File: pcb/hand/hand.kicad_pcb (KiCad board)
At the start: 2 copper layers, 149.5 x 99.8 mm, 35 parts, among them J1 Conn_01x15, J2 Conn_01x15

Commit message: pcb/hand Begin tidying DRC.
TODO:
- Name
- Date
- Connect J1 to J2
- Finish DRC
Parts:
- renumbered REF** to H1, REF** to H2, REF** to H3, REF** to H4
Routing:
- net col5: track 91.3 -> 121.7 mm
- net col1: track 173.0 -> 198.4 mm
- net col3: track 133.1 -> 158.6 mm
- net col2: track 159.3 -> 184.7 mm
- net col4: track 121.8 -> 147.1 mm
- net col0: track 167.1 -> 186.2 mm
- net row2: track 162.9 -> 176.7 mm
- net row3: track 185.7 -> 197.7 mm
- net row0: track 184.5 -> 193.6 mm
- net row1: track 148.1 -> 157.0 mm
- net col6: track 45.1 -> 52.3 mm

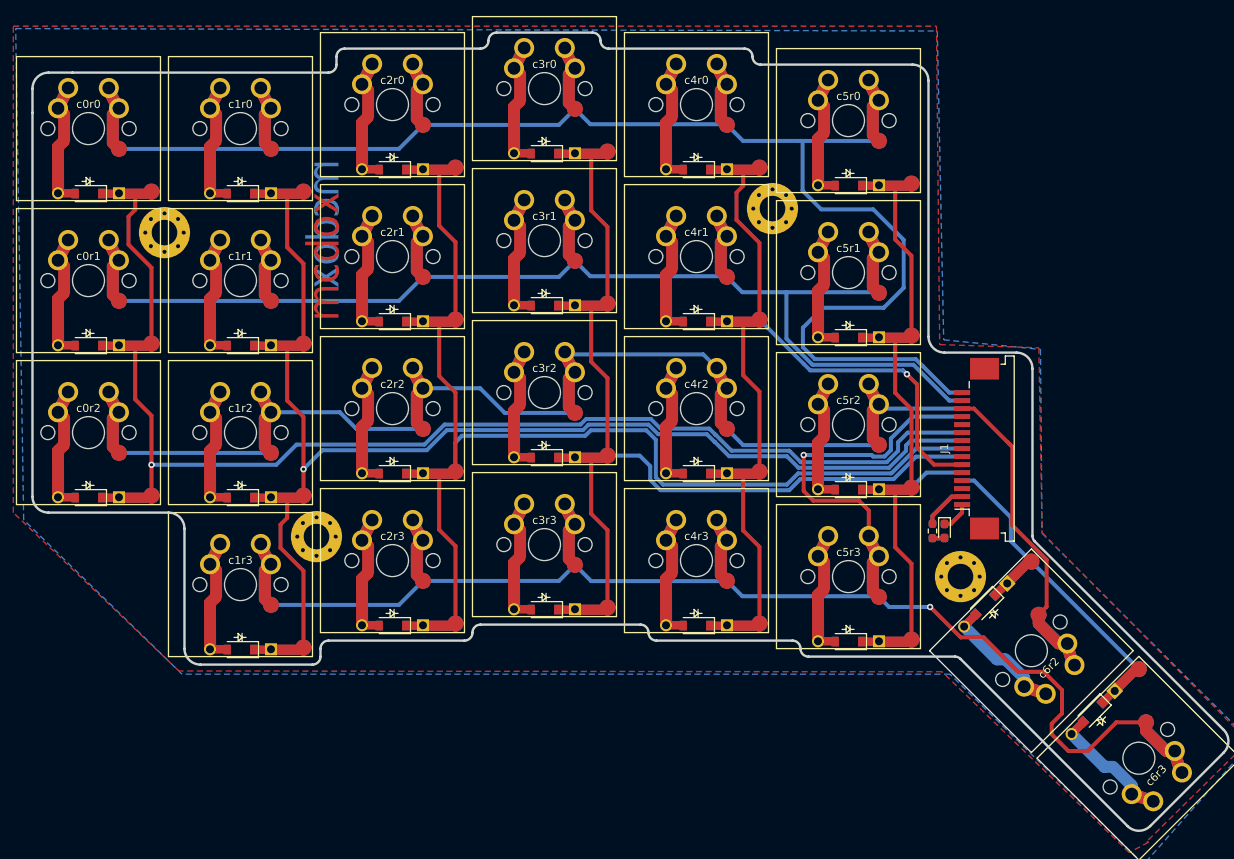
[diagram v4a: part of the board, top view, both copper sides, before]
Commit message: pcb/hand Recess cutout under switches on Eco2.User
Remove all the pad-to-pad tracks too... Loads of them!
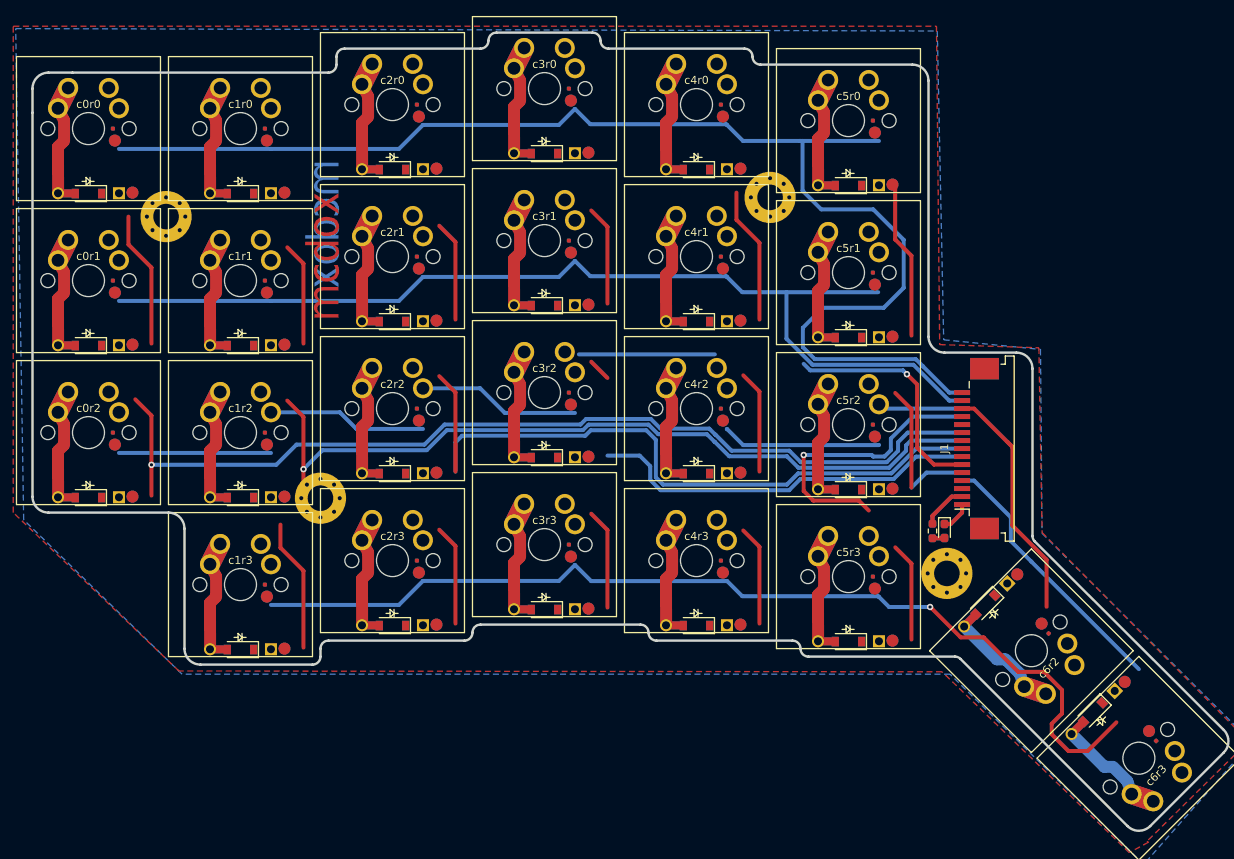
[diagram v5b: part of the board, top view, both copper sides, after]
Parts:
- H1, H2, H3, H4: footprint MountingHole:MountingHole_3.2mm_M3_Pad_Via -> hand:MountingHole_3.2mm_M3_Pad_Via
- moved H2 4.83 mm to (36.0, 53.2)
- moved H1 2.01 mm to (16.7, 18.0)
- moved H4 1.75 mm to (114.3, 62.6)
- moved H3 1.43 mm to (92.2, 15.6)
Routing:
- net col3: track 158.6 -> 76.8 mm
- net col4: track 147.1 -> 72.1 mm
- net col2: track 184.7 -> 113.0 mm
- net col5: track 121.7 -> 51.8 mm
- net col1: track 198.4 -> 130.8 mm
- net col0: track 186.2 -> 138.0 mm
- net row2: track 176.7 -> 136.5 mm
- net row3: track 197.7 -> 160.4 mm
- net row0: track 193.6 -> 165.5 mm
- net row1: track 157.0 -> 129.6 mm
- net col6: track 52.3 -> 33.6 mm

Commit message: pcb/hand Full layout.
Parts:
- moved R1 4.33 mm to (113.0, 53.0), turned to 180 degrees
- moved R2 4.33 mm to (113.0, 53.0), turned to 180 degrees
- moved LED1 2.97 mm to (113.0, 54.5), turned to 180 degrees
- moved LED2 2.97 mm to (113.0, 54.5), turned to 180 degrees
- moved H4 0.40 mm to (114.3, 63.0)
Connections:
- J1 pad 11: (no net) -> row4_NC
- J1 pad 3: (no net) -> col7_NC
- J2 pad 13: (no net) -> col7_NC
- J2 pad 5: (no net) -> row4_NC
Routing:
- net row2: track 136.5 -> 237.7 mm, vias 0 -> 1
- net row3: track 160.4 -> 246.1 mm, vias 2 -> 3
- net col3: track 76.8 -> 155.6 mm, vias 0 -> 1
- net row1: track 129.6 -> 208.1 mm, vias 0 -> 1
- net col4: track 72.1 -> 142.4 mm, vias 1 -> 2
- net col2: track 113.0 -> 177.4 mm, vias 0 -> 1
- net col1: track 130.8 -> 194.8 mm
- net col5: track 51.8 -> 112.7 mm, vias 0 -> 1
- net row0: track 165.5 -> 216.8 mm, vias 0 -> 1
- net col0: track 138.0 -> 185.6 mm
- net col6: track 33.6 -> 55.0 mm, vias 0 -> 1
- net row4_NC: track 0.00 -> 3.60 mm, vias 0 -> 1
- net col7_NC: track 0.00 -> 3.60 mm, vias 0 -> 1
- net +3V3: track 11.4 -> 9.18 mm, vias 0 -> 1
- net GND: track 7.58 -> 8.66 mm, vias 0 -> 1
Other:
- board text added: "Dave McEwan"
- board text added: "Feb 2023"

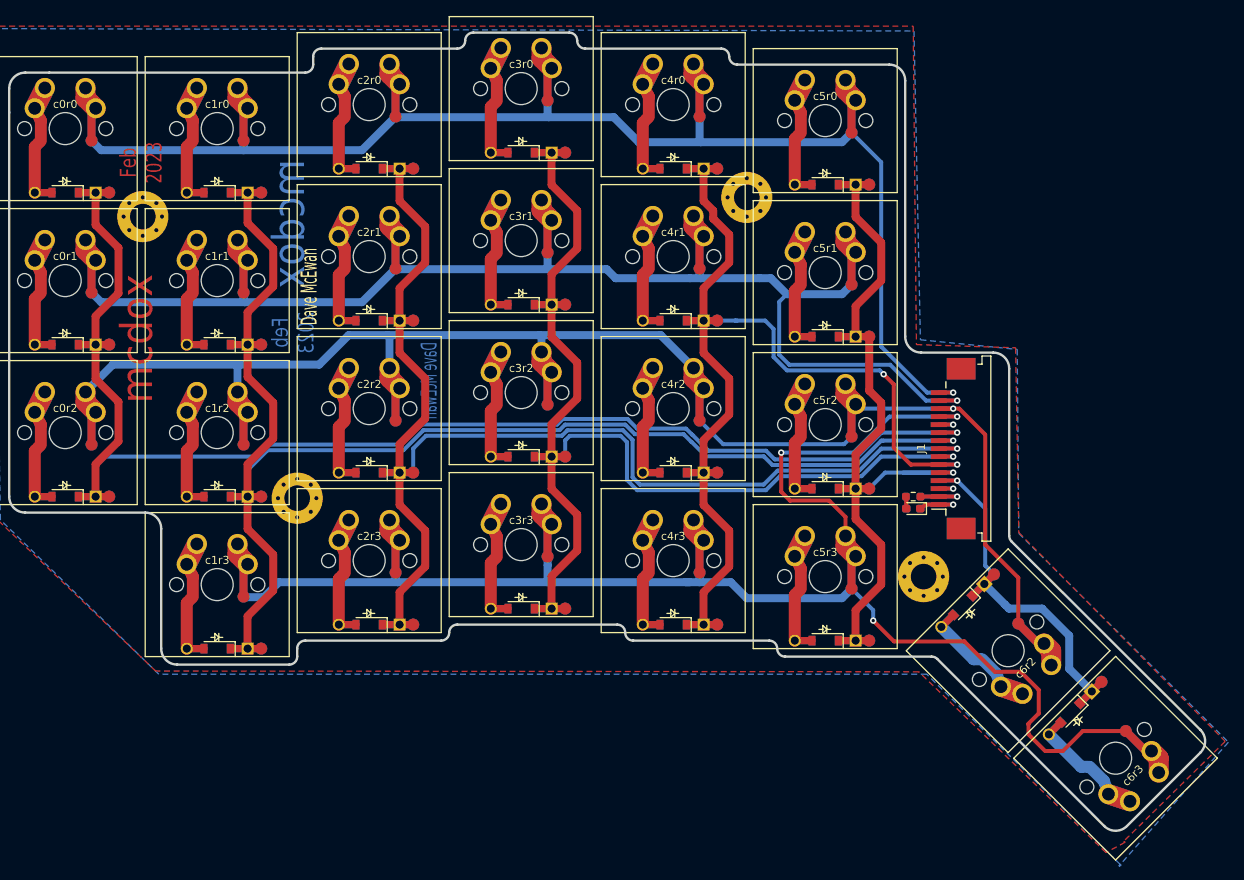
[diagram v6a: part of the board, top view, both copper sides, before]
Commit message: case PCB and outline placement.
Can fit all 5 layers on a single 400x600mm sheet.
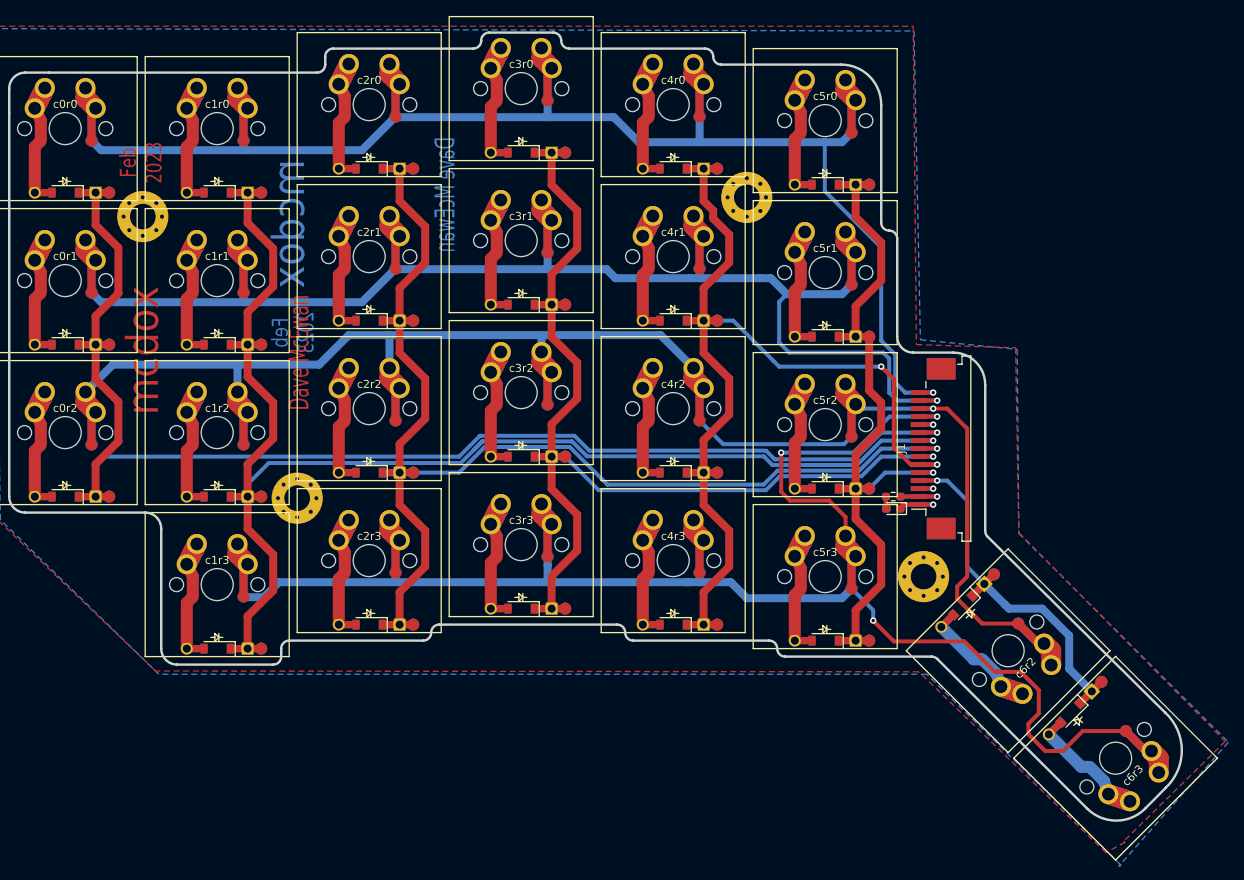
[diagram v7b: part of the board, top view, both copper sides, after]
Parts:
- moved J1 2.50 mm to (115.5, 47.0)
- moved J2 2.50 mm to (115.5, 47.0)
- moved LED1 2.50 mm to (110.5, 54.5)
- moved LED2 2.50 mm to (110.5, 54.5)
- moved R1 2.50 mm to (110.5, 53.0)
- moved R2 2.50 mm to (110.5, 53.0)
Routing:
- net col2: track 177.4 -> 168.7 mm
- net col3: track 155.6 -> 147.0 mm
- net col5: track 112.7 -> 105.7 mm
- net col0: track 185.6 -> 181.3 mm
- net col1: track 194.8 -> 191.5 mm
- net row3: track 246.1 -> 243.6 mm
- net col6: track 55.0 -> 57.3 mm
- net row2: track 237.7 -> 239.8 mm
- net col4: track 142.4 -> 140.5 mm
- net row1: track 208.1 -> 207.2 mm
- net row0: track 216.8 -> 216.1 mm
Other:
- board size 149.5 x 99.8 mm -> 146.6 x 98.5 mm
